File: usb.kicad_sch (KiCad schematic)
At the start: 130 parts, among them J3 USB-C_USB4105-GF-A, J4 Conn_USB-C_WE_632723300011, U10 TUSB1046-DCIRNQ, U11 TPD4E05U06QDQARQ1, U12 AP22615A_TSOT26, U13 TPD4E05U06QDQARQ1, U14 TPD4E05U06QDQARQ1, U15 TPD4E05U06QDQARQ1, U16 TPD4E05U06QDQARQ1, U5 FT230X_QFN, U6 TPS65988DHRSHR, U7 W25Q80DV_USON, U8 NCP730BMT330_WSON, U9 AP22615A_TSOT26

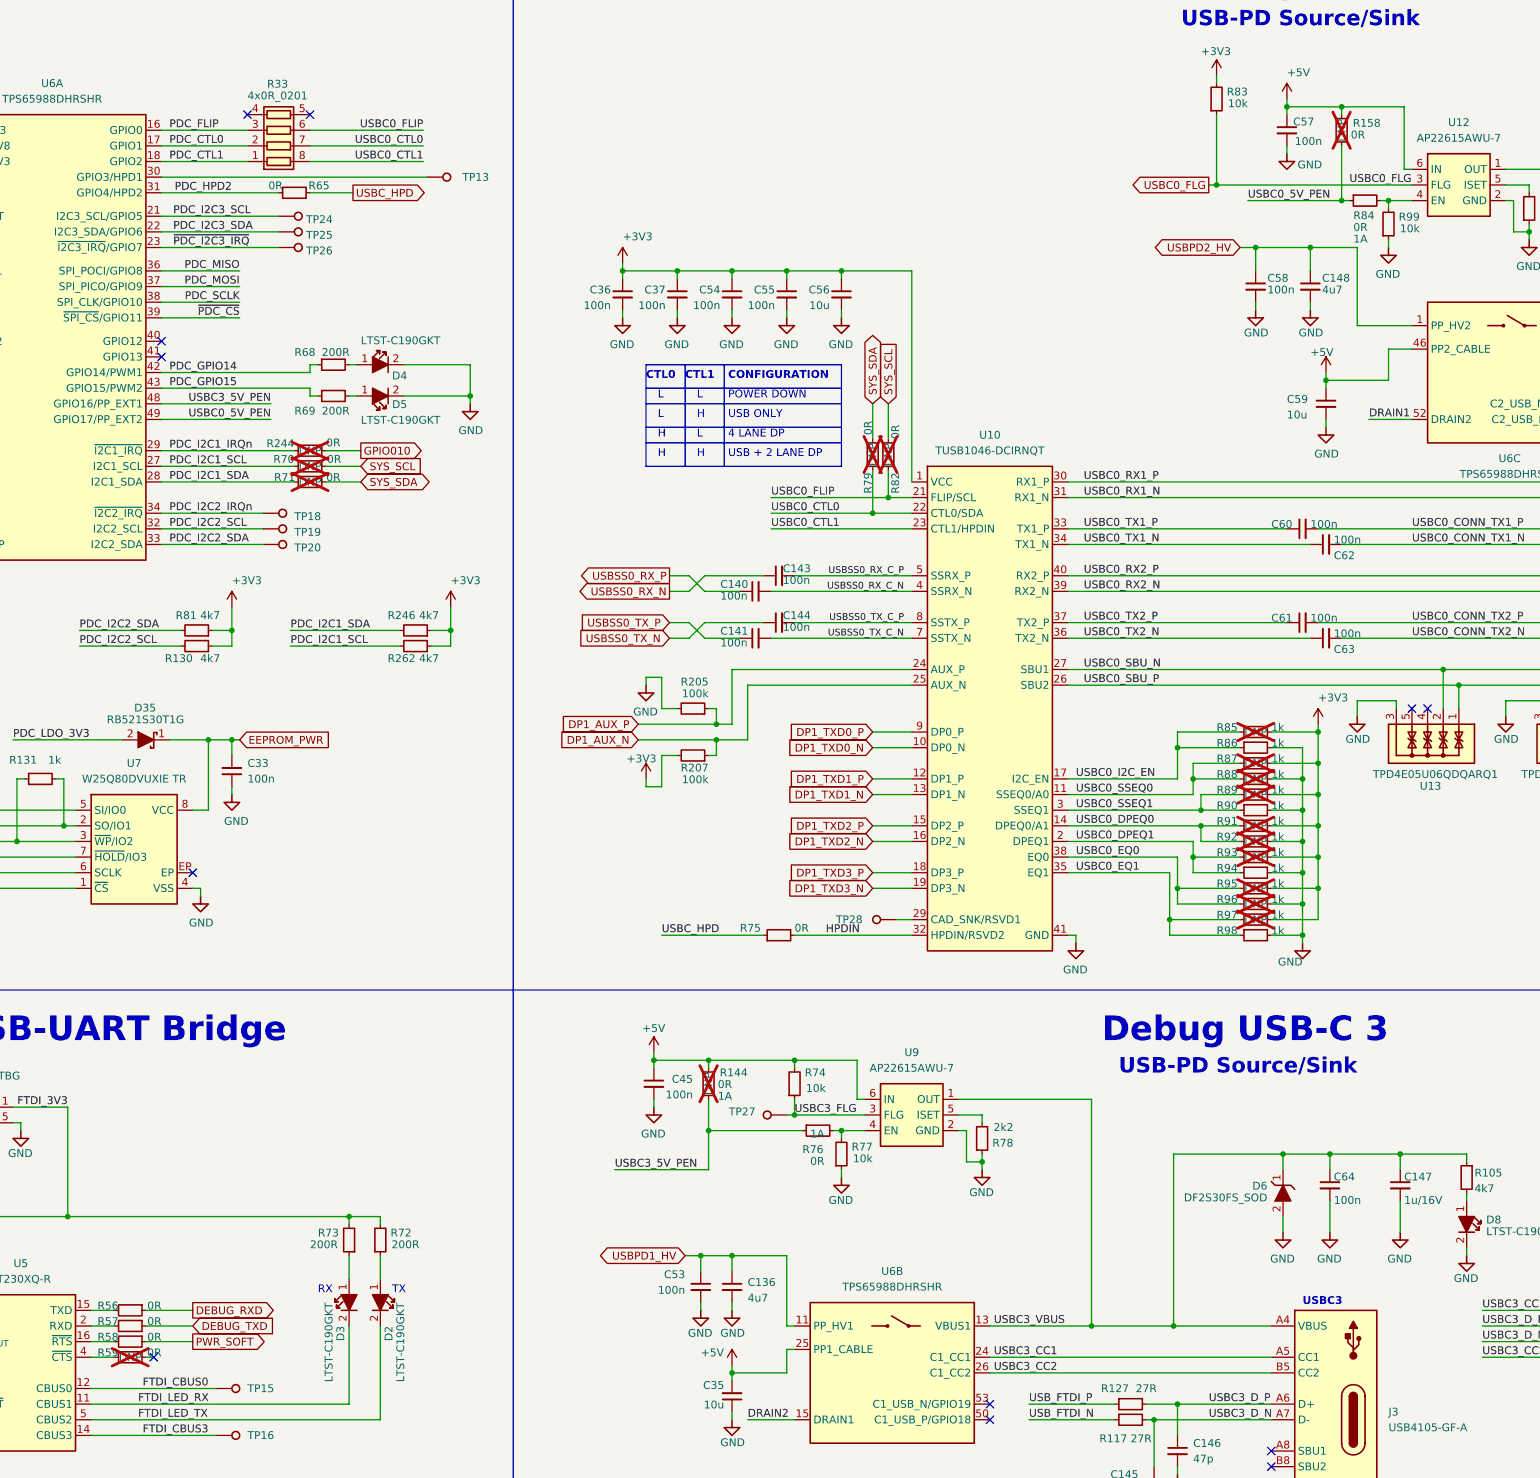
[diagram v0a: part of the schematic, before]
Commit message: 5/16 Commit: Sch Mods added and beginning Development on PCB layout
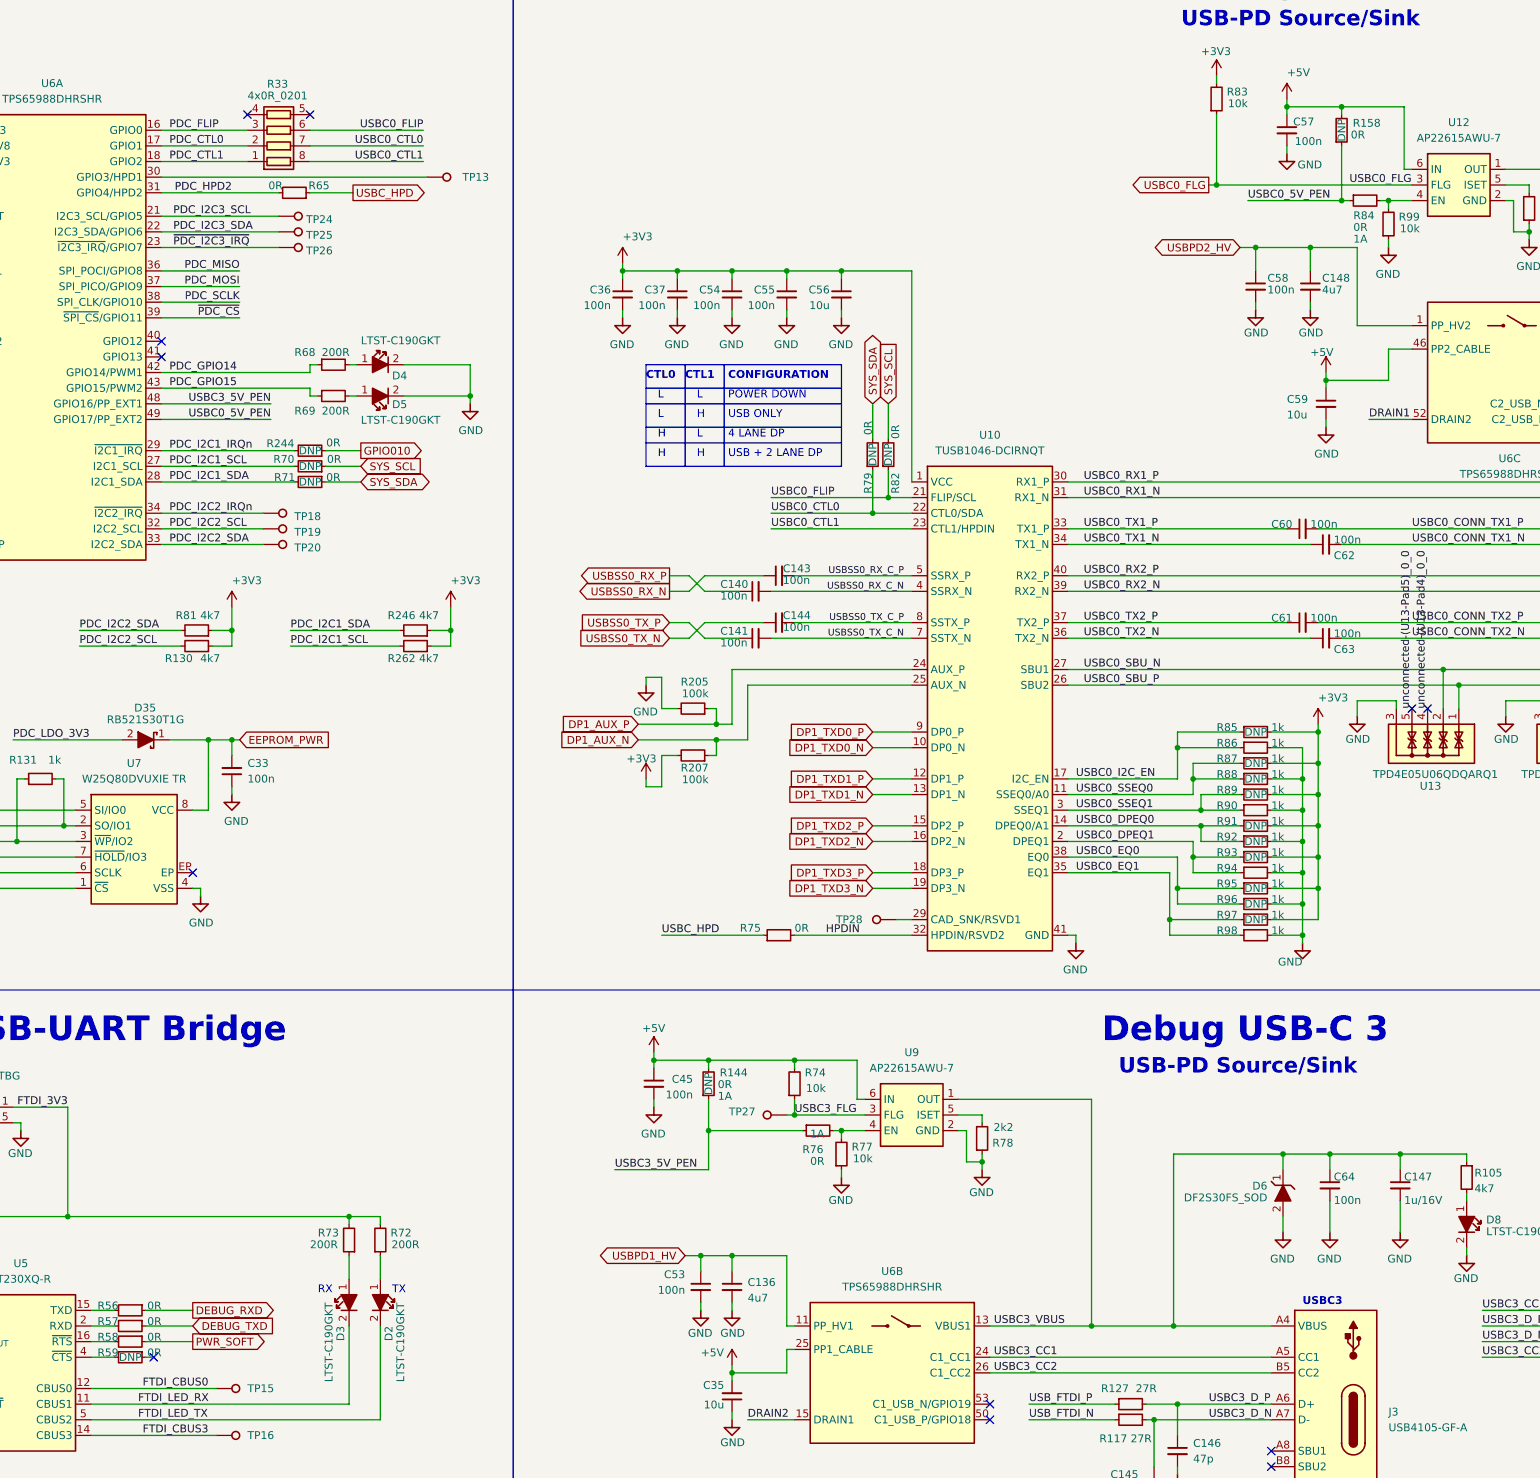
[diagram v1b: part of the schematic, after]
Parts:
- R144, R158, R244, R59, R70, R71, R79, R82, R85, R87, R88, R89, R91, R92, R93, R95, R96, R97: now fitted
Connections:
- net unconnected-(U13-Pad4)_0_0: now reaches U13.4, U13.7
- net unconnected-(U13-Pad5)_0_0: now reaches U13.5, U13.6
